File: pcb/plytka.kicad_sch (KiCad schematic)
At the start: 40 parts, among them J1 Display, J2 Program, J3 Battery, J4 hanxia HX TYPE-C 6P L5.0, SW1 RESET, SW2 USER1, SW3 USER2, SW4 USER3, U2 TP4054

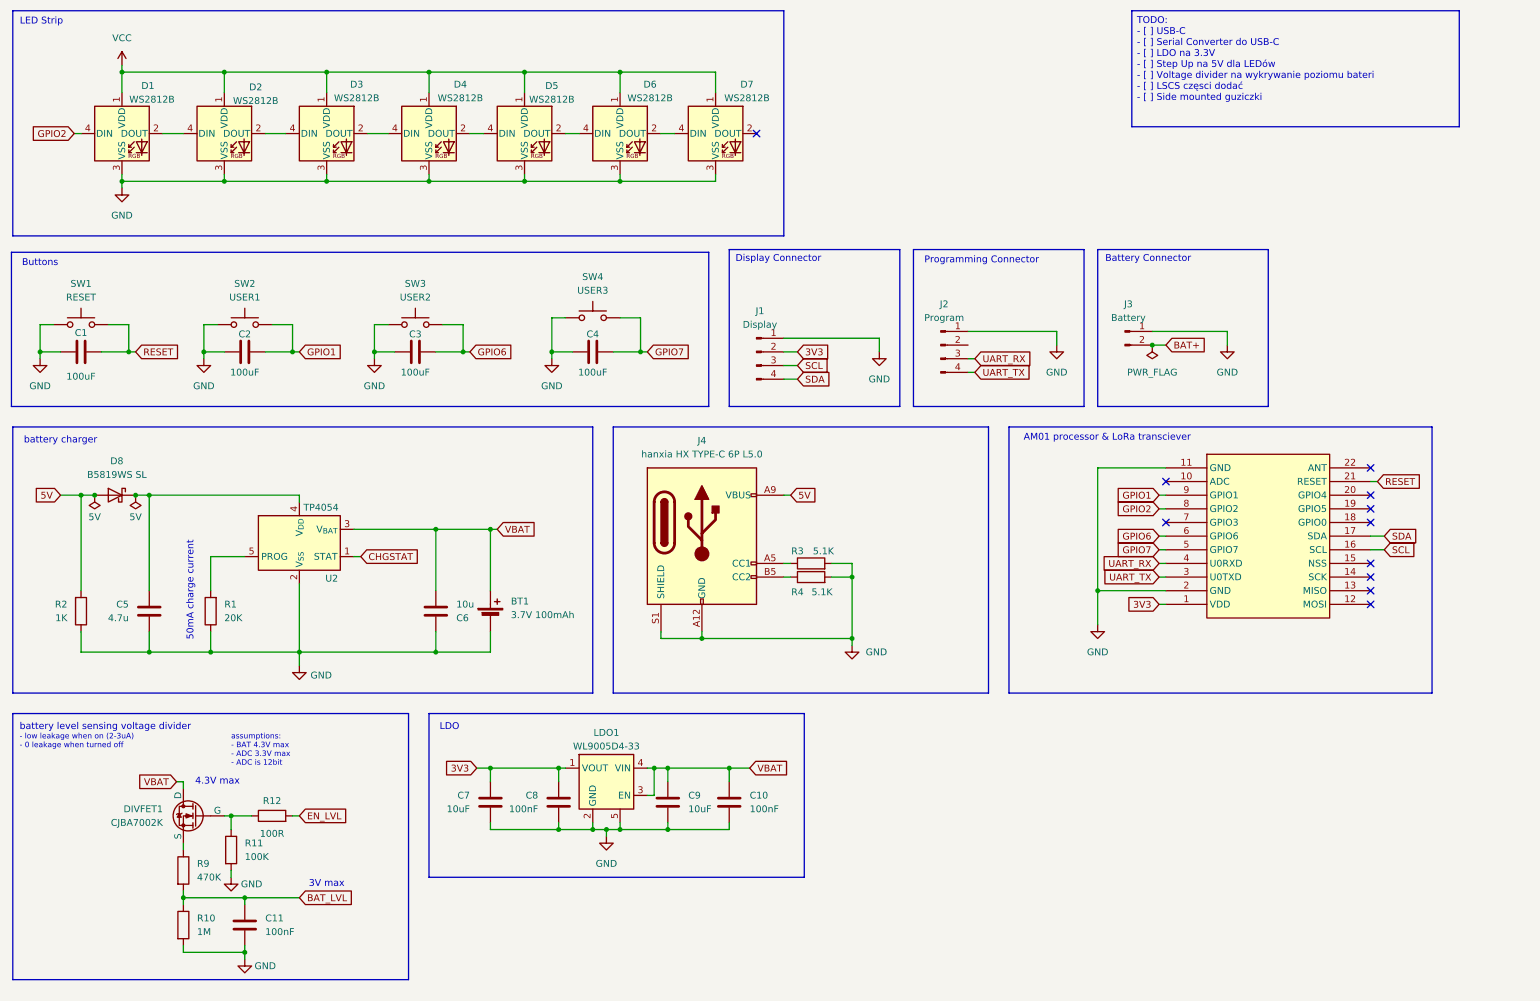
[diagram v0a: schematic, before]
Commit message: pcb: add TPS61022 boost converter and simplify battery monitoring
- Add TPS61022 boost converter
- Simplify battery voltage sensing by removing DIVFET1 switched divider
- Update voltage divider values, now 1M and 1M + cap for stabilizing
- Add mode selection jumper for PFM/PWM switching
- Update battery capacity to ~500mAh
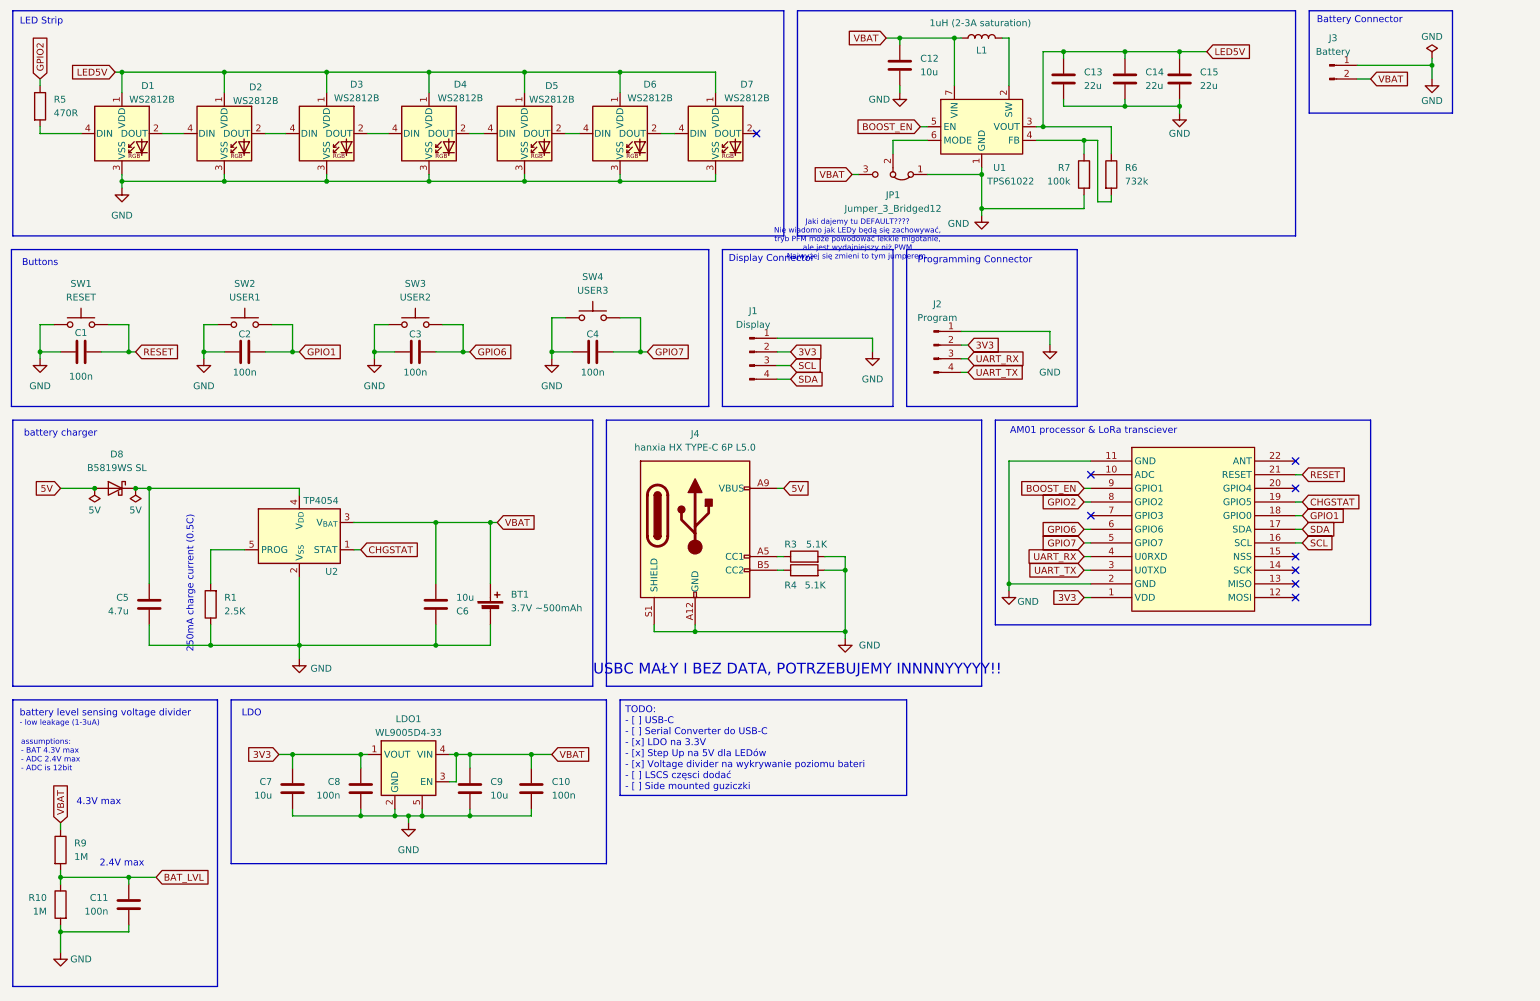
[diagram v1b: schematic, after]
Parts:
- removed DIVFET1: CJBA7002K, Library:DFN1006-3L, symbol Simulation_SPICE:NMOS
- removed R11: 100K, Resistor_SMD:R_0201_0603Metric, symbol Device:R
- removed R12: 100R, Resistor_SMD:R_0201_0603Metric, symbol Device:R
- removed R2: 1K, Resistor_SMD:R_0201_0603Metric, symbol Device:R
- added C12: 10u, symbol Device:C
- added C13, C14, C15: 22u, symbol Device:C
- added JP1: Jumper_3_Bridged12, symbol Jumper:Jumper_3_Bridged12
- added L1: 1uH (2-3A saturation), symbol Device:L
- added R5: 470R, symbol Device:R
- added R6: 732k, symbol Device:R
- added R7: 100k, symbol Device:R
- added U1: TPS61022, Package_DFN_QFN:Texas_RWU0007A_VQFN-7_2x2mm_P0.5mm, symbol Converter_DCDC:TPS61022
- BT1: value 3.7V 100mAh -> 3.7V ~500mAh
- C1, C2, C3, C4: value 100uF -> 100n
- C10, C11, C8: value 100nF -> 100n
- C7, C9: value 10uF -> 10u
- R1: value 20K -> 2.5K
- R9: value 470K -> 1M
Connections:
- net BAT+ is gone; now on net VBAT: J3.2 (Pin_2)
- net 3V3: now also J2.2 (Pin_2)
- net CHGSTAT: now also HTCC-AM1.19 (GPIO5)
- net GND: now also C12.2, C13.2, C14.2, C15.2, JP1.1 (A), R7.2, U1.1 (GND)
- net GPIO1: now also HTCC-AM1.18 (GPIO0); no longer HTCC-AM1.9 (GPIO1)
- net GPIO2: now also R5.1; no longer D1.4 (DIN)
- net VBAT: now also R9.1, C12.1, JP1.3 (B), L1.1, U1.7 (VIN)
- net VCC renamed LED5V
- net LED5V: now also C13.1, C14.1, C15.1, R6.1, U1.3 (VOUT)
- new net: D1.4 (DIN), R5.2
- new net: R6.2, R7.1, U1.4 (FB)
- new net: L1.2, U1.2 (SW)
- new net: JP1.2 (C), U1.6 (MODE)
- new net BOOST_EN: HTCC-AM1.9 (GPIO1), U1.5 (EN)
- no-connect marks 11 -> 9
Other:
- note added: "- low leakage (1-3uA)"
- note added: "2.4V max"
- note added: "250mA charge current (0.5C)"
- note added: "Jaki dajemy tu DEFAULT???? Nie wiadomo jak LEDy będą się zachowywać, tryb PFM może powodować lekkie migotanie, ale jest wydajniejszy niż PWM Najwyżej się zmieni to tym jumperem."
- note added: "USBC MAŁY I BEZ DATA, POTRZEBUJEMY INNNNYYYYY!!"
- note added: "assumptions: - BAT 4.3V max - ADC 2.4V max - ADC is 12bit"
- note removed: "- low leakage when on (2-3uA) - 0 leakage when turned off"
- note removed: "3V max"
- note removed: "50mA charge current"
- note removed: "assumptions: - BAT 4.3V max - ADC 3.3V max - ADC is 12bit"
- moved on the sheet: C10, C5, C6, C7, C8, C9, D8, J1, J2, J3, J4, LDO1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

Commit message: aktualna wersja
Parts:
- removed J4: hanxia HX TYPE-C 6P L5.0, Library:USB-C-HANXIA-6P-BS-5.0, symbol Connector:USB_C_Receptacle_PowerOnly_6P
- removed R4: 5.1K, Resistor_SMD:R_0201_0603Metric, symbol Device:R
- added C16: 10 uF, Capacitor_SMD:C_0805_2012Metric, symbol Device:C
- added C17, C18: 100n, Capacitor_SMD:C_0402_1005Metric, symbol Device:C
- added D9: D_Schottky, Diode_SMD:D_SMA, symbol Device:D_Schottky
- added J4: USB_C_Receptacle_USB2.0_16P, Connector_USB:USB_C_Receptacle_G-Switch_GT-USB-7010ASV, symbol Connector:USB_C_Receptacle_USB2.0_16P
- added Q1, Q2: SS8050, Package_TO_SOT_SMD:SOT-23, symbol Transistor_BJT:SS8050
- added R11: 10k, Resistor_SMD:R_01005_0402Metric, symbol Device:R
- added R12: 10k, Resistor_SMD:R_0402_1005Metric, symbol Device:R
- added R2: 5.1 k, Resistor_SMD:R_0603_1608Metric, symbol Device:R
- added U3: USBLC6-2P6, Package_TO_SOT_SMD:SOT-666, symbol Power_Protection:USBLC6-2P6
- added U4: CH340K, Package_SO:SSOP-10-1EP_3.9x4.9mm_P1mm_EP2.1x3.3mm, symbol Interface_USB:CH340K
- R3: value 5.1K -> 5.1k; footprint Resistor_SMD:R_0201_0603Metric -> Resistor_SMD:R_0603_1608Metric
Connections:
- net 3V3: now also C18.1, U4.7 (VCC)
- net 5V: now also C16.1, D9.2 (A)
- net BOOST_EN: now also Q1.3 (C)
- net GND: now also R3.1, C16.2, C17.2, C18.2, J4.A1 (GND), J4.A12 (GND), J4.B1 (GND), J4.B12 (GND), J4.S1 (SHIELD), R2.1, U3.2 (GND), U4.11 (GND), U4.3 (GND); no longer R3.2
- net RESET: now also Q2.3 (C)
- net UART_RX: now also U4.9 (RXD)
- net UART_TX: now also U4.8 (TXD)
- new net: Q2.1 (B), R12.2
- new net: D9.1 (K), J4.A4 (VBUS), J4.A9 (VBUS), J4.B4 (VBUS), J4.B9 (VBUS), U3.5 (VBUS)
- new net: J4.A5 (CC1), R2.2, U3.6 (I/O1)
- new net: J4.B5 (CC2), R3.2, U3.4 (I/O2)
- new net: C17.1, U4.10 (V3)
- new net: Q1.1 (B), R11.2
- new net D+: J4.A6 (D+), J4.B6 (D+), U3.3 (I/O2), U4.1 (UD+)
- new net D-: J4.A7 (D-), J4.B7 (D-), U3.1 (I/O1), U4.2 (UD-)
- new net DTR: Q2.2 (E), R11.1, U4.4 (~{DTR})
- new net RTS: Q1.2 (E), R12.1, U4.6 (~{RTS})
- no-connect marks 9 -> 12
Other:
- note added: "logic converter"
- note added: "usb to uart converter"
- note added: "usb-c"
- note removed: "USBC MAŁY I BEZ DATA, POTRZEBUJEMY INNNNYYYYY!!"
